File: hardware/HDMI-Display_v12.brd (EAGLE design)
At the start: 52 x 52 mm, 105 parts, among them IC1 TFP401A-PAD, IC2 24LC02B, IC3 IS31BL3506A-TTLS2, IC4 ATMEGA32U4-MU, IC5 VREG-TS1117CW-3V3, J20_1 JUMPER2-0402, J20_2 JUMPER2-0402, J30_1 JUMPER2-0402, J30_2 JUMPER2-0402, Q1 16MHz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

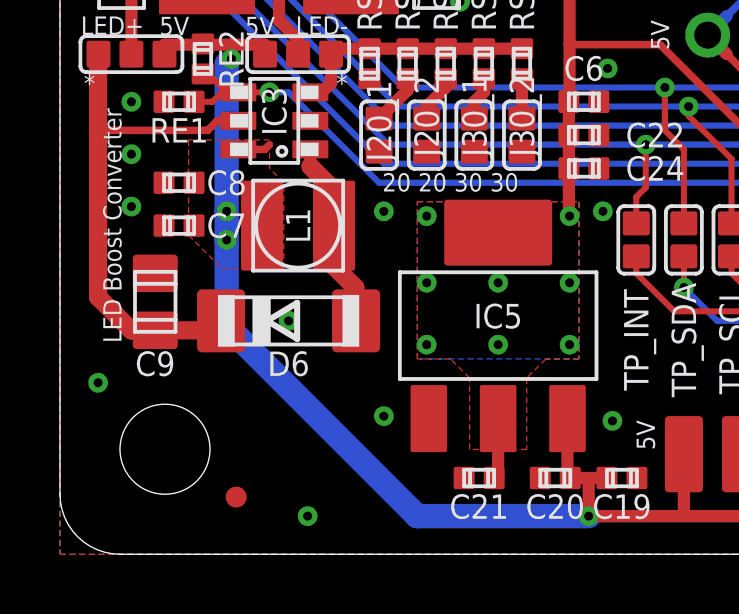
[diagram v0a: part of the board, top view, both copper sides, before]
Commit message: updated schematics
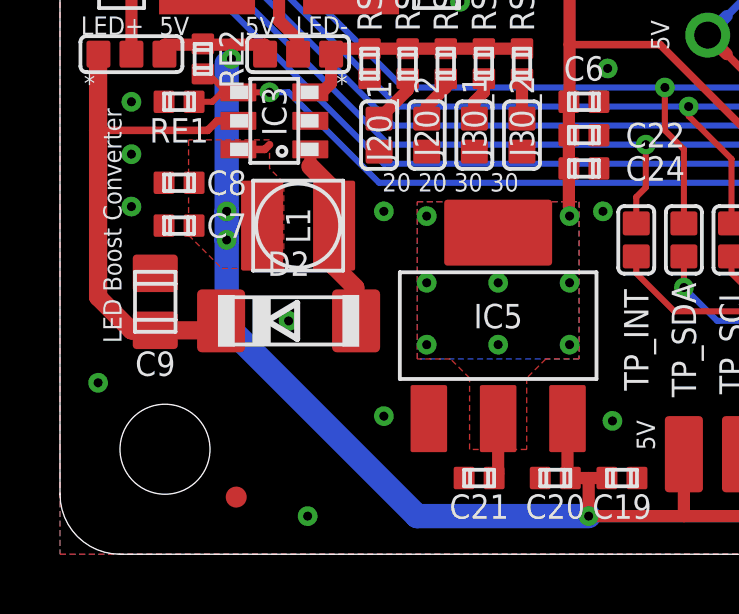
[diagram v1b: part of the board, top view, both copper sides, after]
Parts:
- C7: value 2u -> 4u7
- C9: value 1u @ 40V -> 1u/40V
- D2: value DIODE-SOD106 -> 40V/0.5A-SOD106
- L1: value 10u@500mA -> 10u/0.5A
- renumbered D6 to D2
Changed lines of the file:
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@@
 <attribute name="VALUE" x="4.60375" y="14.44625" size="0.8128" layer="27" font="vector" ratio="10" rot="R90" align="center"/>
 </element>
-<element name="L1" library="we-power" package="L_1212" value="10u@500mA" x="7.9375" y="10.95375" smashed="yes" rot="R90">
+<element name="L1" library="we-power" package="L_1212" value="10u/0.5A" x="7.9375" y="10.95375" smashed="yes" rot="R90">
 <attribute name="NAME" x="7.9375" y="10.95375" size="0.8128" layer="25" font="vector" ratio="10" rot="R90" align="center"/>
 <attribute name="VALUE" x="7.9375" y="9.04875" size="0.8128" layer="27" font="vector" ratio="10" align="center"/>
-</element>
-<element name="D6" library="we-rcl" package="SOD106" value="DIODE-SOD106" x="7.62" y="7.77875" smashed="yes" rot="R90">
-<attribute name="NAME" x="7.62" y="6.35" size="0.8128" layer="25" font="vector" ratio="10" align="center"/>
-<attribute name="VALUE" x="7.62" y="5.87375" size="0.8128" layer="27" font="vector" ratio="10" align="center"/>
 </element>
 <element name="RS2" library="we-rcl" package="C0402" value="15" x="11.58875" y="16.35125" smashed="yes" rot="R180">
@@
 <attribute name="VALUE" x="10.31875" y="16.35125" size="0.8128" layer="27" font="vector" ratio="10" rot="R90" align="center"/>
 </element>
-<element name="C9" library="we-rcl" package="C0805" value="1u @ 40V" x="3.175" y="8.41375" smashed="yes">
+<element name="C9" library="we-rcl" package="C0805" value="1u/40V" x="3.175" y="8.41375" smashed="yes">
 <attribute name="NAME" x="3.175" y="6.35" size="0.8128" layer="25" font="vector" ratio="10" align="center"/>
 <attribute name="VALUE" x="4.7625" y="8.41375" size="0.8128" layer="27" font="vector" ratio="10" rot="R270" align="center"/>
@@
 <attribute name="VALUE" x="4.1275" y="12.3825" size="0.8128" layer="27" font="vector" ratio="10" align="center"/>
 </element>
-<element name="C7" library="we-rcl" package="C0402" value="2u" x="3.96875" y="10.95375" smashed="yes" rot="R90">
+<element name="C7" library="we-rcl" package="C0402" value="4u7" x="3.96875" y="10.95375" smashed="yes" rot="R90">
 <attribute name="NAME" x="5.55625" y="10.95375" size="0.8128" layer="25" font="vector" ratio="10" align="center"/>
 <attribute name="VALUE" x="4.1275" y="10.95375" size="0.8128" layer="27" font="vector" ratio="10" align="center"/>
@@
 <attribute name="DIGIKEY" value="CKN10511DKR-ND" x="50.4" y="10.5" size="1.778" layer="27" rot="R90" display="off"/>
 </element>
+<element name="D2" library="we-rcl" package="SOD106" value="40V/0.5A-SOD106" x="7.62" y="7.77875" rot="R90"/>
 </elements>
 <signals>
@@
 <signal name="LED+">
 <contactref element="IC3" pad="5"/>
-<contactref element="D6" pad="C"/>
 <contactref element="C9" pad="2"/>
 <wire x1="1.27" y1="16.66875" x2="1.27" y2="14.12875" width="0.6096" layer="1"/>
@@
 <contactref element="LED+" pad="1"/>
 <wire x1="1.27" y1="16.66875" x2="1.28125" y2="16.66875" width="0.2032" layer="1"/>
+<contactref element="D2" pad="C"/>
 </signal>
 <signal name="LIGHT">
@@
 <contactref element="L1" pad="2"/>
 <contactref element="IC3" pad="1"/>
-<contactref element="D6" pad="A"/>
 <wire x1="8.34375" y1="13.49625" x2="8.34375" y2="12.92875" width="0.4064" layer="1"/>
 <wire x1="8.34375" y1="12.92875" x2="9.04875" y2="12.22375" width="0.6096" layer="1"/>
@@
 <wire x1="9.8425" y1="8.89" x2="9.8425" y2="7.80625" width="0.6096" layer="1"/>
 <wire x1="9.8425" y1="7.80625" x2="9.87" y2="7.77875" width="0.2032" layer="1"/>
+<contactref element="D2" pad="A"/>
 </signal>
 <signal name="X+">
